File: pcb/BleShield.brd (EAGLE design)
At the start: 23 parts, among them U1 ARDUINO_SHIELDNOHOLES, Y1 32.768KHz, 10 PPM

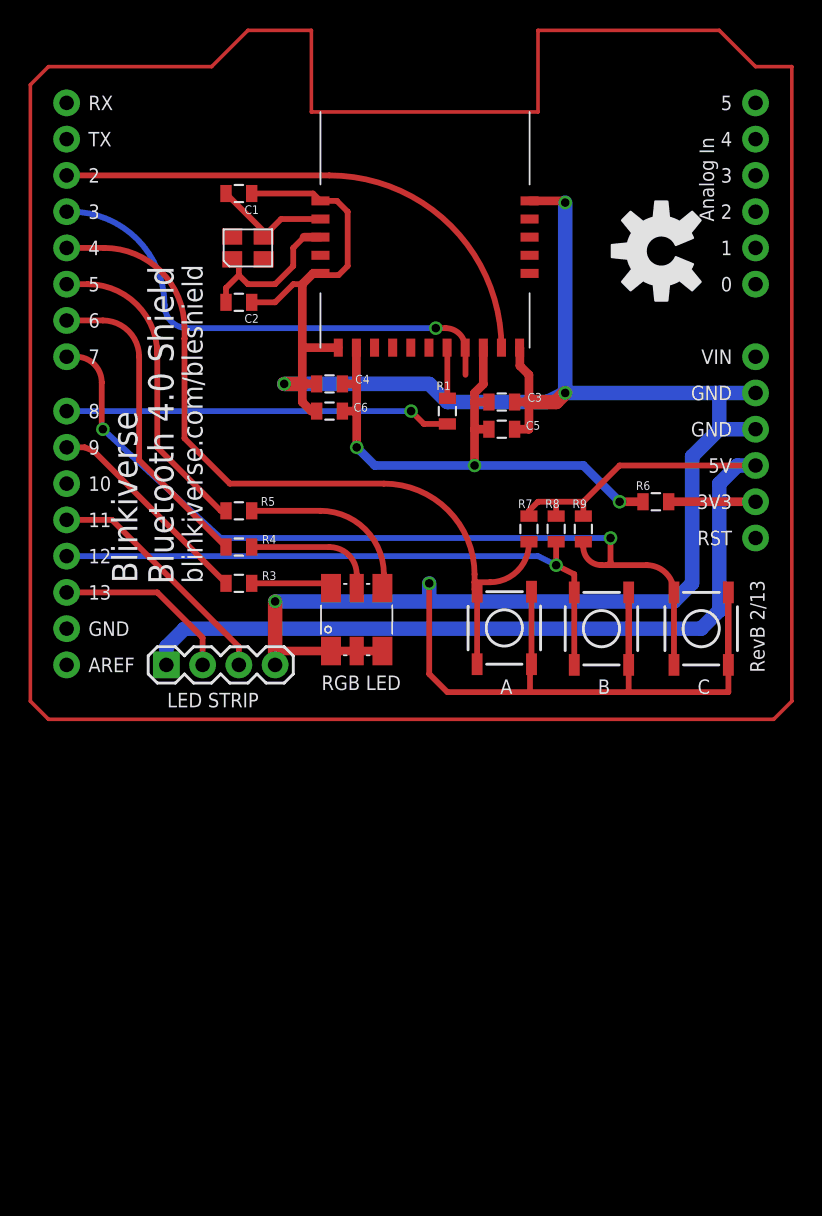
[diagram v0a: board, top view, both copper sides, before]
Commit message: fixed LED strip header, minor re-routing
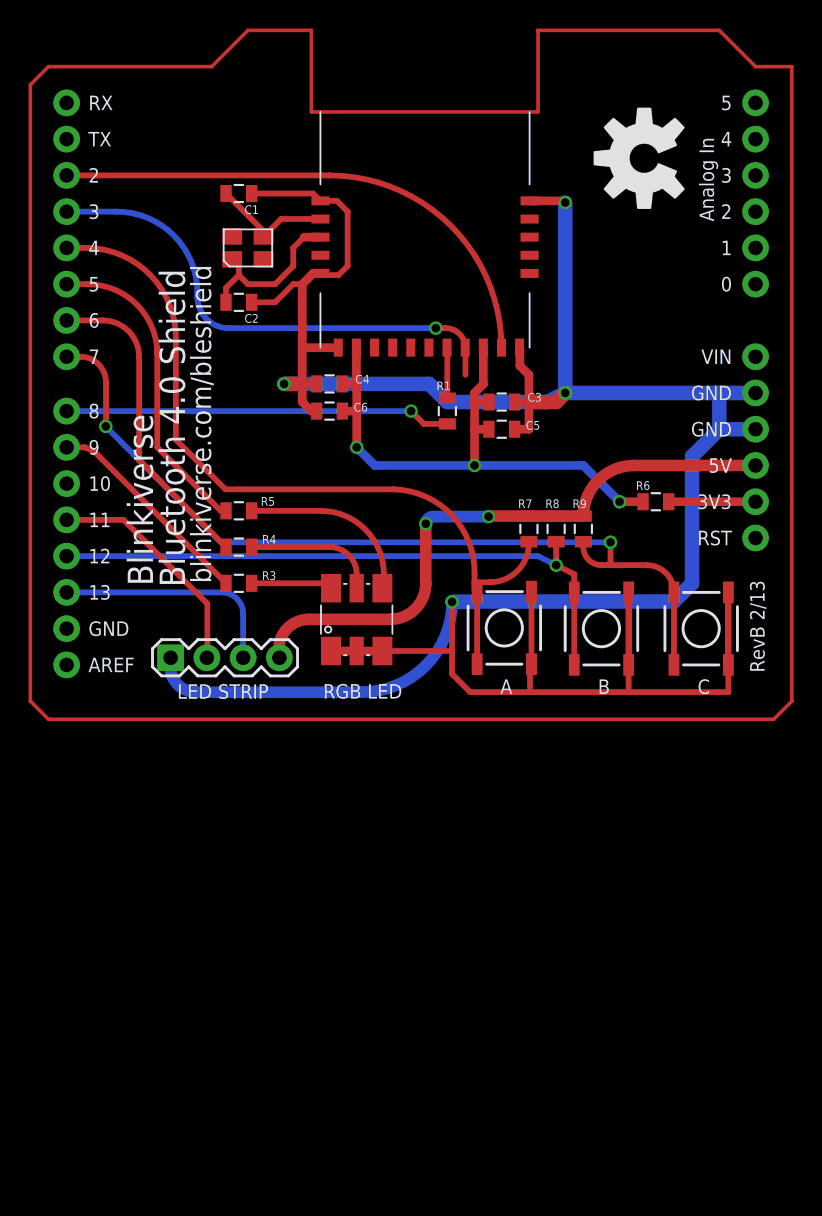
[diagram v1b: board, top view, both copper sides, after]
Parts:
- moved U$7 6.61 mm to (43.0, 39.3)
- moved LED STRIP 0.58 mm to (9.82, 4.31)
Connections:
- net 5V: now also LED STRIP.4; no longer LED STRIP.1
- net GND: now also LED STRIP.1; no longer LED STRIP.4
- net MOSI: now also LED STRIP.2; no longer LED STRIP.3
- net SCK: now also LED STRIP.3; no longer LED STRIP.2
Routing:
- net 5V: track 72.6 -> 41.8 mm, vias 0 -> 2
- net GND: track 212.8 -> 219.6 mm, vias 5 -> 4
- net SCK: track 12.7 -> 16.1 mm
- net MOSI: track 17.0 -> 16.1 mm

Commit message: Update documentation, layout
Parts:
- moved R5 1.27 mm to (14.6, 13.3)
- moved R4 0.63 mm to (14.6, 11.4)
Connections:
- net GND: now also U1.GND@2
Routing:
- net GND: track 219.6 -> 27.0 mm, vias 4 -> 0
- net LED_GREEN: track 22.0 -> 23.0 mm
- net N$5: track 12.1 -> 11.2 mm
- net N$17: track 209.4 -> 210.2 mm
- added copper zone on layer 1, net GND
- added copper zone on layer 16, net GND

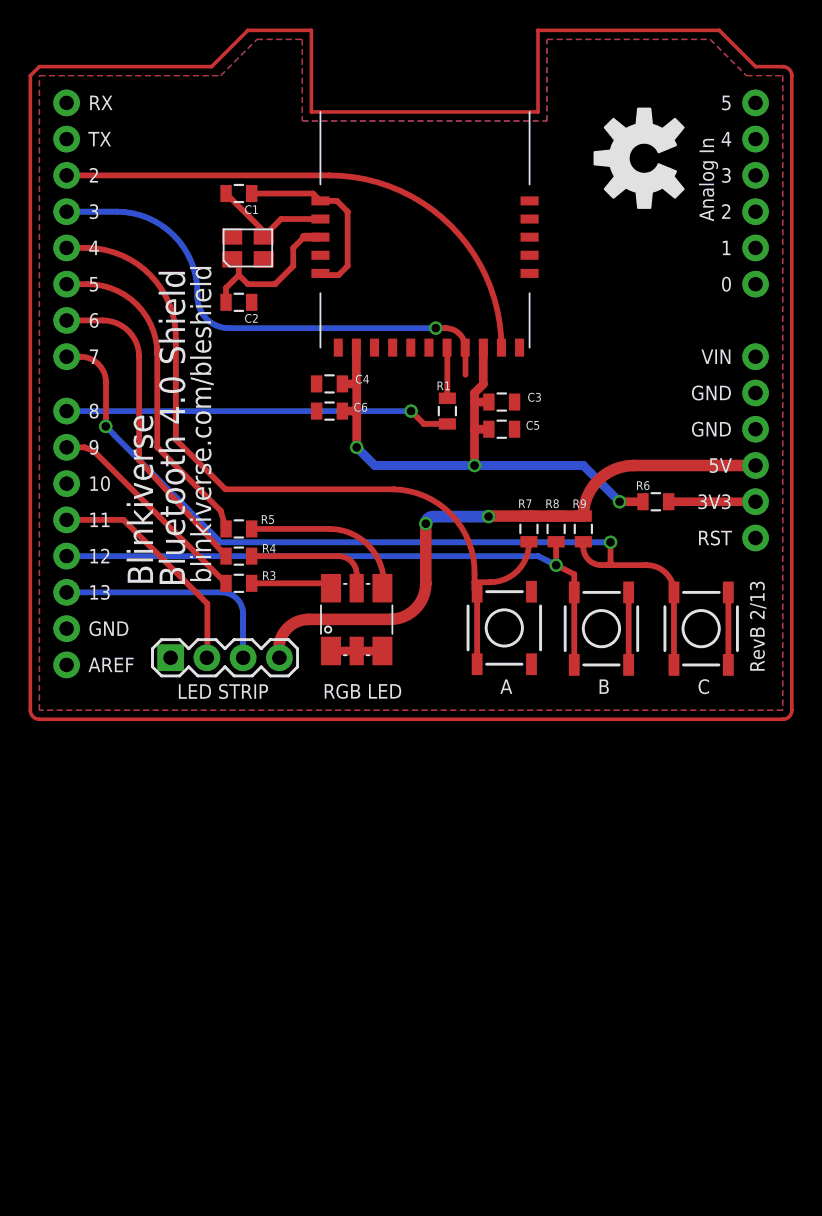
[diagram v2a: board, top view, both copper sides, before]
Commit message: Add keepaway, cutout to BLE part, knock out some to-do items.
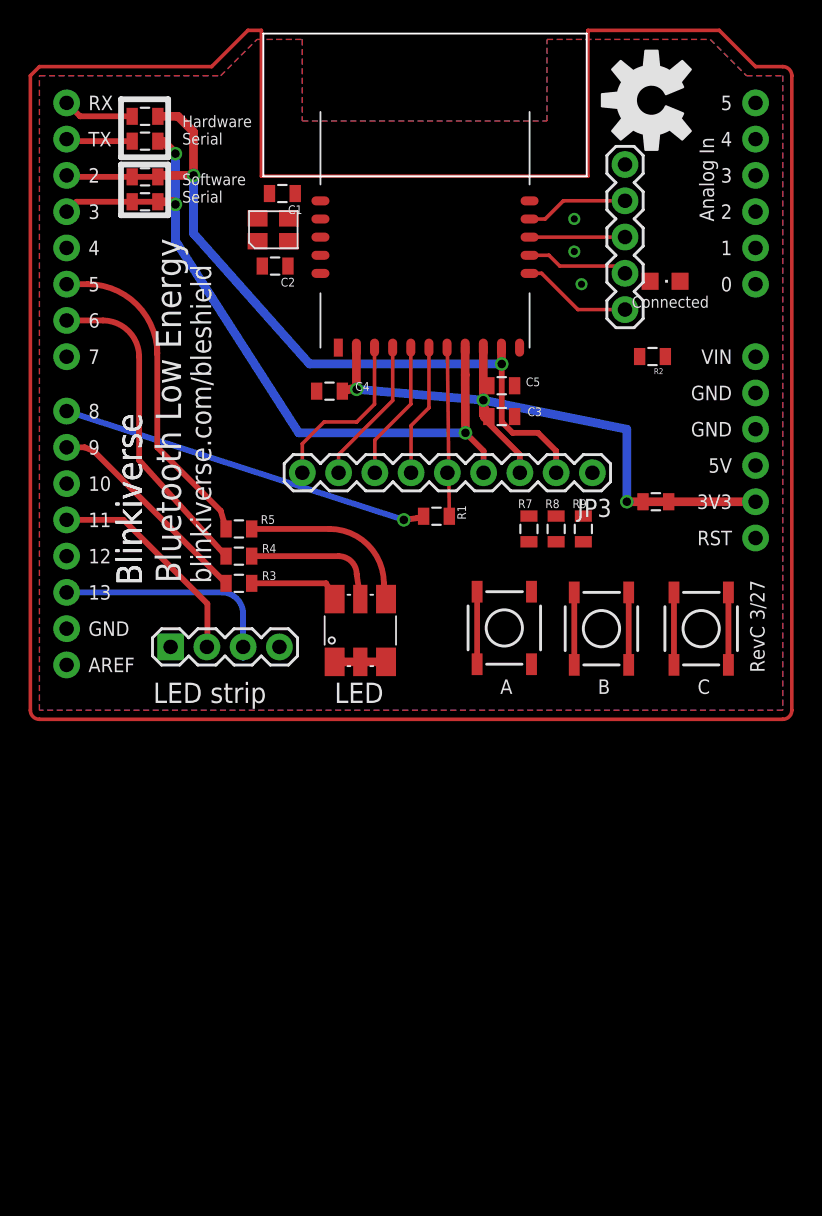
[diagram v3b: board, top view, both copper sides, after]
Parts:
- removed C6: 100nf, SparkFun:0805
- removed LED STRIP: (no value), SparkFun:1X04
- removed RGB LED: LED-TRICOLOR-5050", blinkiverse:LED-TRICOLOR-5050-FIXED
- added JP2: (no value), SparkFun:1X05
- added JP3: M09, SparkFun:1X09
- added LED1: (no value), adafruit:CHIPLED_0805
- added LED_STRIP: (no value), SparkFun:1X04
- added R10, R11, R12, R13: DNP, SparkFun:0805
- added R2: 470, SparkFun:0805
- added RGB_LED: LED-TRICOLOR-5050", blinkiverse:LED-TRICOLOR-5050-FIXED
- C3: value 10uf -> 220uF 6.3V
- C4: value 10uf -> 100nF
- C5: value 100nf -> 100nF
- R3, R4, R5: value 330 -> 470
- R6: value 0 -> DNP
- moved R1 7.41 mm to (28.4, 14.2), turned to 0 degrees
- moved U$7 4.10 mm to (43.5, 43.4)
- moved C2 3.59 mm to (17.1, 31.8)
- moved C1 3.05 mm to (17.7, 36.8)
- moved C5 3.05 mm to (33.0, 23.4)
- moved Y1 2.18 mm to (17.0, 34.3)
- moved C3 1.02 mm to (33.0, 21.2)
- moved C4 0.51 mm to (21.0, 23.0)
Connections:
- new net N$10: R10.1, U1.RX
- new net N$11: R11.1, U1.TX
- new net N$12: JP3.8, U$1.P2_1
- new net N$13: JP3.7, U$1.P1_4/CT
- new net N$14: JP3.6, U$1.P1_5/RT
- new net N$15: JP2.2, U$1.P0_4
- new net N$16: JP2.3, U$1.P0_5
- new net N$18: JP2.4, U$1.P0_6
- new net N$7: LED1.A, R2.1
- new net N$9: JP2.5, R2.2, U$1.P0_7
- net 3.3V: now also C3.2, C4.2, C5.2, JP3.3, R6.2, U$1.VDD_1, U$1.VDD_2
- net 5V: now also LED_STRIP.4; no longer LED STRIP.4
- net GND: now also JP2.1, JP3.1, LED1.C, LED_STRIP.1, RGB_LED.1, RGB_LED.2, RGB_LED.3; no longer C6.1, LED STRIP.1, RGB LED.1, RGB LED.2, RGB LED.3
- net MOSI: now also LED_STRIP.2; no longer LED STRIP.2
- net N$1: now also JP3.5
- net N$2: now also RGB_LED.6; no longer RGB LED.6
- net N$5: now also RGB_LED.4; no longer RGB LED.4
- net N$6: now also RGB_LED.5; no longer RGB LED.5
- net N$8: now also JP3.9, U$1.P2_2; no longer C3.2, C4.2, C5.2, C6.2, R6.2, U$1.VDD_1, U$1.VDD_2
- net RX: now also JP3.2, R10.2, R12.1, R12.2
- net SCK: now also LED_STRIP.3; no longer LED STRIP.3
- net SWITCH_A: now also U1.D12; no longer U1.D4
- net SWITCH_B: now also U1.D4; no longer U1.D12
- net TX: now also JP3.4, R11.2, R13.1, R13.2
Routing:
- net SWITCH_C: track 60.1 -> 5.08 mm, vias 2 -> 0
- net SWITCH_A: track 53.7 -> 5.08 mm
- net 3.3V: track 6.08 -> 49.4 mm, vias 0 -> 3
- net 5V: track 41.8 -> 0.00 mm, vias 2 -> 0
- net SWITCH_B: track 43.8 -> 5.08 mm, vias 1 -> 0
- net N$8: track 41.2 -> 12.2 mm, vias 3 -> 0
- net RX: track 35.5 -> 56.1 mm, vias 0 -> 2
- net TX: track 34.0 -> 52.7 mm, vias 1 -> 3
- net GND: track 27.0 -> 13.9 mm, vias 0 -> 3
- net N$4: track 11.7 -> 0.00 mm
- net N$12: track 0.00 -> 10.3 mm
- net N$13: track 0.00 -> 9.81 mm
- net N$14: track 0.00 -> 9.28 mm
- net N$17: track 210.2 -> 219.2 mm
- net N$3: track 8.59 -> 0.00 mm
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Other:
- board outline added: 22.6 x 10 mm
- board text added: "Bluetooth Low Energy"
- board text added: "Connected"
- board text added: "Hardware Serial"
- board text added: "LED"
- board text added: "LED strip"
- board text added: "RevC 3/27"
- board text added: "Software Serial"
- board text removed: "Bluetooth 4.0 Shield"
- board text removed: "RevB 2/13"

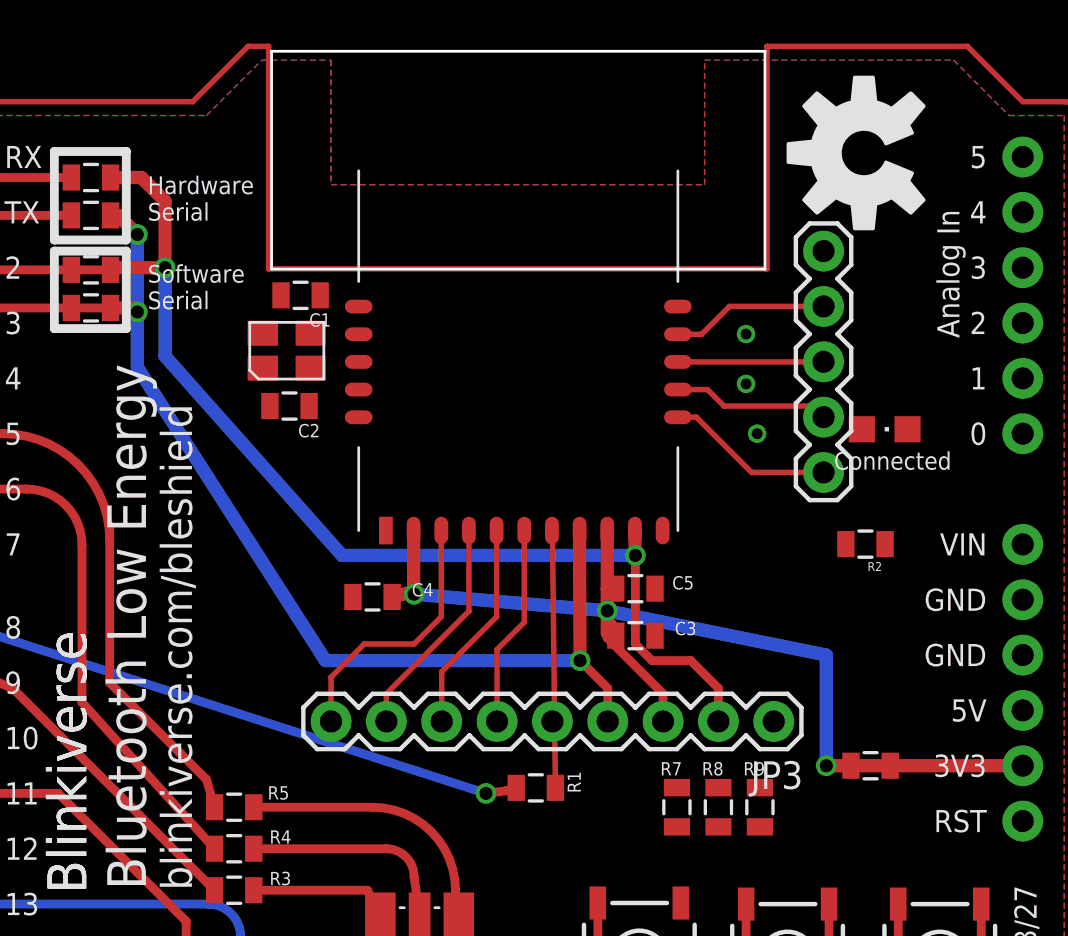
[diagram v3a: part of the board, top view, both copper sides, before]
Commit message: Swap out programming headers to 1.27mm, to match module pitch (only a master will use these anyway?)
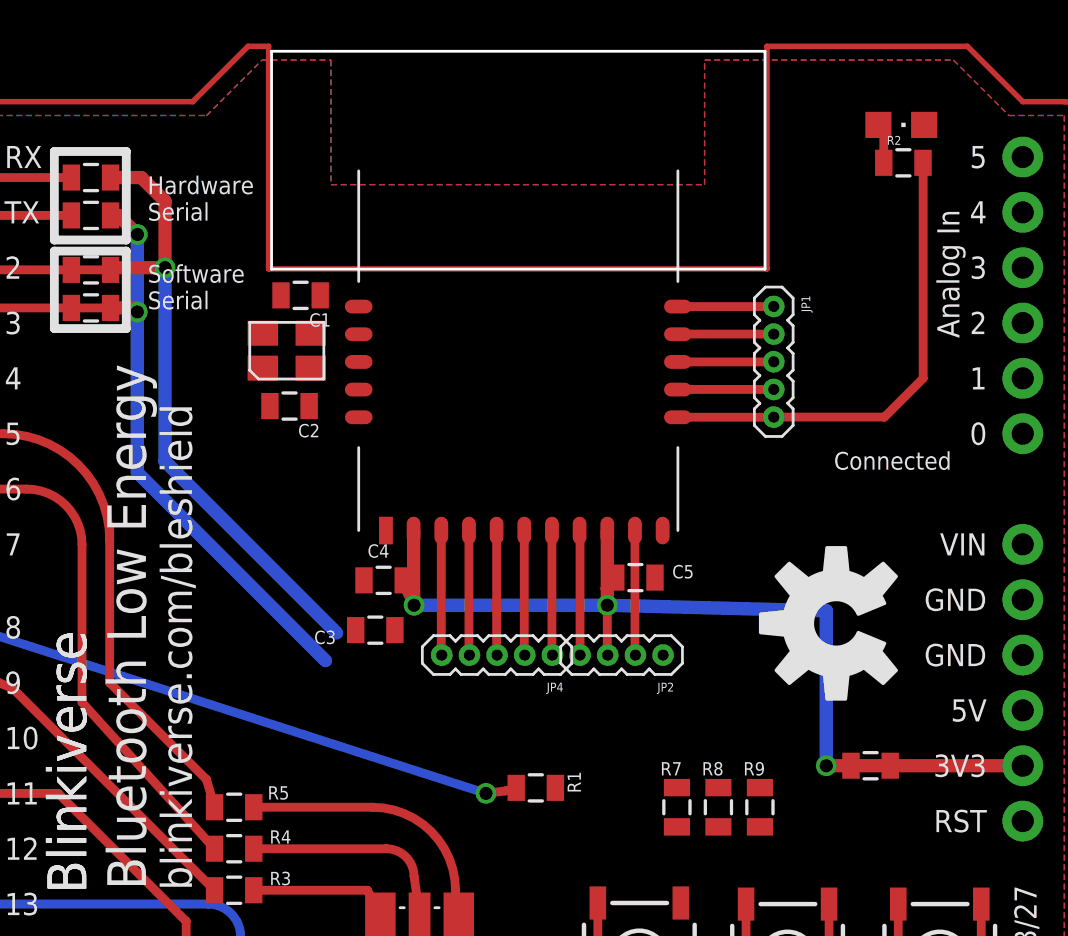
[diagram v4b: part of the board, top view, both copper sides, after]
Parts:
- removed JP3: M09, SparkFun:1X09
- added JP1, JP4: (no value), SparkFun:1X05-1.27MM
- JP2: device SparkFun:1X05 -> SparkFun:1X04-1.27MM
- moved U$7 21.6 mm to (42.2, 21.8)
- moved JP2 20.0 mm to (34.3, 20.3), turned to 180 degrees
- moved R2 17.6 mm to (45.3, 42.9), turned to 0 degrees
- moved LED1 14.0 mm to (45.2, 44.7)
- moved C3 11.9 mm to (21.1, 21.5), turned to 0 degrees
- moved C4 0.92 mm to (21.5, 23.7)
- moved C5 0.51 mm to (33.0, 23.9)
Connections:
- net 3.3V: now also JP2.3; no longer JP3.3
- net GND: now also JP1.1; no longer JP3.1
- net N$1: now also JP4.1; no longer JP3.5
- net N$12: now also JP4.4; no longer JP3.8
- net N$13: now also JP4.3; no longer JP3.7
- net N$14: now also JP4.2; no longer JP3.6
- net N$15: now also JP1.2; no longer JP2.2
- net N$16: now also JP1.3; no longer JP2.3
- net N$18: now also JP1.4; no longer JP2.4
- net N$8: now also JP4.5; no longer JP3.9
- net N$9: now also JP1.5; no longer JP2.5
- net RX: now also JP2.2; no longer JP3.2
- net TX: now also JP2.4; no longer JP3.4
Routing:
- net RX: track 56.1 -> 40.7 mm, vias 2 -> 1
- net TX: track 52.7 -> 38.4 mm, vias 3 -> 2
- net N$9: track 7.74 -> 21.9 mm
- net N$8: track 12.2 -> 5.72 mm
- net N$1: track 11.8 -> 5.74 mm
- net N$12: track 10.3 -> 5.72 mm
- net GND: track 13.9 -> 18.3 mm, vias 3 -> 0
- net N$13: track 9.81 -> 5.72 mm
- net N$14: track 9.28 -> 5.72 mm
- net 3.3V: track 49.4 -> 46.0 mm
- net N$15: track 7.21 -> 4.41 mm
- net N$18: track 7.21 -> 4.41 mm
- net N$16: track 6.69 -> 4.41 mm
- net N$7: track 0.00 -> 1.84 mm
